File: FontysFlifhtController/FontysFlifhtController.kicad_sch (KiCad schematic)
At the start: 28 parts, among them J1 Conn_01x04, J10 Motor Control 3, J11 Motor Control 4, J12 Ultrasonic Sensor, J13 Battery Power, J2 Conn_01x04, J3 Conn_01x04, J4 Conn_01x04, J5 Conn_01x04, J6 Camera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

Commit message: Flight controller v2.0
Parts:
- removed C1: 4700uF, Capacitor_THT:CP_Radial_D13.0mm_P5.00mm, symbol Device:C_Polarized
- removed D1: LED_RGBA, LED_THT:LED_D5.0mm-4_RGB_Wide_Pins, symbol Device:LED_RGBA
- removed J3, J4, J5: Conn_01x04, Connector_JST:JST_PH_S4B-PH-K_1x04_P2.00mm_Horizontal, symbol Connector_Generic:Conn_01x04
- removed Q1: IRLZ34N, Package_TO_SOT_THT:TO-220-3_Vertical, symbol Simulation_SPICE:NMOS
- removed R2: 82, Resistor_THT:R_Axial_DIN0207_L6.3mm_D2.5mm_P7.62mm_Horizontal, symbol Device:R
- removed R3, R4: 12, Resistor_THT:R_Axial_DIN0207_L6.3mm_D2.5mm_P7.62mm_Horizontal, symbol Device:R
- removed SW1: Switch, Connector_PinHeader_2.54mm:PinHeader_1x03_P2.54mm_Vertical, symbol FlightController:Switch_APEM2
- removed U1: 4R7_Buck_Converter, FlightController:4R7_Buck_Converter, symbol FlightController:4R7_Buck_Converter
- added D1, D3, D4, D5: SS24, Diode_SMD:D_SOD-123F, symbol Diode:PMEG1020EH
- added D2: WS2812B (LED), LED_SMD:LED_WS2812B_PLCC4_5.0x5.0mm_P3.2mm, symbol LED:WS2812B
- added J14: RaspberryPi, Connector_PinHeader_2.54mm:PinHeader_1x01_P2.54mm_Vertical, symbol Connector_Generic:Conn_01x01
- added J3: SPI 1, Connector_JST:JST_PH_S6B-PH-K_1x06_P2.00mm_Horizontal, symbol Connector_Generic:Conn_01x06
- added J4: SPI 2, Connector_JST:JST_PH_S6B-PH-K_1x06_P2.00mm_Horizontal, symbol Connector_Generic:Conn_01x06
- J1: value Conn_01x04 -> I2C 1
- J2: value Conn_01x04 -> I2C 2
- J6: footprint Connector_JST:JST_EH_S5B-EH_1x05_P2.50mm_Horizontal -> Connector_JST:JST_PH_S5B-PH-K_1x05_P2.00mm_Horizontal
- R1: value R -> 1M; footprint Resistor_THT:R_Axial_DIN0207_L6.3mm_D2.5mm_P7.62mm_Horizontal -> Resistor_SMD:R_0805_2012Metric
- U2: footprint RF_Module:nRF24L01_Breakout -> Connector_PinHeader_2.54mm:PinHeader_2x04_P2.54mm_Vertical
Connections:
- net A6: now also J12.1 (Pin_1); no longer J12.3 (Pin_3)
- net D10: now also U2.4 (~{CSN}); no longer J6.2 (Pin_2)
- net D11: now also U2.6 (MOSI), J3.4 (Pin_4), J4.4 (Pin_4)
- net D12: now also U2.7 (MISO), J3.3 (Pin_3), J4.3 (Pin_3)
- net D13: now also U2.5 (SCK), J3.2 (Pin_2), J4.2 (Pin_2)
- net D3: now also J6.3 (Pin_3); no longer U2.3 (CE)
- net D4: now also J6.4 (Pin_4); no longer U2.4 (~{CSN})
- net D5: now also D2.4 (DIN); no longer U2.5 (SCK)
- net D6: now also J3.1 (Pin_1); no longer U2.6 (MOSI)
- net D7: now also J4.1 (Pin_1); no longer U2.7 (MISO)
- net D9: now also U2.3 (CE); no longer J6.3 (Pin_3)
- net GND: now also J12.3 (Pin_3), D2.3 (VSS), J3.6 (Pin_6), J4.6 (Pin_6); no longer J12.1 (Pin_1)
- net VIN: now reaches J13.1 (Pin_1)
- net VIN: now also A1.30 (VIN)
- net 5V: now reaches R1.2
- net 5V: now also A1.27 (+5V), D1.2 (A), D2.1 (VDD), D3.2 (A), D4.2 (A), D5.2 (A), J14.1 (Pin_1)
- net 3.3V: now reaches A1.17 (3V3)
- net 3.3V: now also J1.2 (Pin_2), J12.2 (Pin_2), J2.2 (Pin_2), J6.5 (Pin_5), J7.4 (Pin_4), U2.2 (VCC), J3.5 (Pin_5), J4.5 (Pin_5)
- net A2: now reaches A1.21 (A2)
- net A2: now also J10.3 (Pin_3)
- net D2: now reaches A1.5 (D2)
- net D2: now also J6.2 (Pin_2)
- net A7: no longer names the net of A1.26 (A7)
- net A7: no longer J10.3 (Pin_3)
- net D8: no longer names the net of A1.11 (D8)
- net D8: no longer J6.4 (Pin_4)
- removed net VCC: A1.30 (VIN), J1.2 (Pin_2), J10.2 (Pin_2), J11.2 (Pin_2), J12.2 (Pin_2), J2.2 (Pin_2), J6.5 (Pin_5), J7.4 (Pin_4), J8.2 (Pin_2), J9.2 (Pin_2), U2.2 (VCC)
- new net: D3.1 (K), J9.2 (Pin_2)
- new net: D4.1 (K), J10.2 (Pin_2)
- new net: D5.1 (K), J11.2 (Pin_2)
- new net: D1.1 (K), J8.2 (Pin_2)
- no-connect marks 9 -> 7
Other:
- note added: "I2C BUS and SPI BUS"
- note removed: "I2C BUS DEVICES"
- moved on the sheet: J13

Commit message: Add turn on/off functionality for the motors
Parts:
- added J5: Motors On/Off, Connector_JST:JST_PH_S4B-PH-K_1x04_P2.00mm_Horizontal, symbol Connector_Generic:Conn_01x04
- D1, D3, D4, D5: LCSC Part # (none) -> C908678
- D2: LCSC Part # (none) -> C2761795
- H1, H2, H3, H4: footprint MountingHole:MountingHole_2.7mm_M2.5 -> MountingHole:MountingHole_3.2mm_M3
- J1, J2: LCSC Part # (none) -> C157926
- J10, J11, J8, J9: LCSC Part # (none) -> C2932698
- J12: LCSC Part # (none) -> C157929
- J13: LCSC Part # (none) -> C474906
- J14: LCSC Part # (none) -> C7501259
- J3, J4: LCSC Part # (none) -> C157920
- J6: LCSC Part # (none) -> C157923
- J7: LCSC Part # (none) -> C2935975
- R1: LCSC Part # (none) -> C17514
- U2: LCSC Part # (none) -> C92271
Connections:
- net D5: now also J5.1 (Pin_1), J5.2 (Pin_2), J5.3 (Pin_3), J5.4 (Pin_4); no longer D2.4 (DIN)
- net A7: now reaches A1.26 (A7)
- net A7: now also D2.4 (DIN)
- no-connect marks 7 -> 6

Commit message: Improve board
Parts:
- removed J5: Motors On/Off, Connector_JST:JST_PH_S4B-PH-K_1x04_P2.00mm_Horizontal, symbol Connector_Generic:Conn_01x04
- added J15: Motor 2 On/Off, Connector_PinHeader_2.54mm:PinHeader_1x03_P2.54mm_Vertical, symbol Connector_Generic:Conn_01x03
- added J16: Motor 3 On/Off, Connector_PinHeader_2.54mm:PinHeader_1x03_P2.54mm_Vertical, symbol Connector_Generic:Conn_01x03
- added J17: Motor 4 On/Off, Connector_PinHeader_2.54mm:PinHeader_1x03_P2.54mm_Vertical, symbol Connector_Generic:Conn_01x03
- added J5: Motor 1 On/Off, Connector_PinHeader_2.54mm:PinHeader_1x03_P2.54mm_Vertical, symbol Connector_Generic:Conn_01x03
- H1, H2, H3, H4: footprint MountingHole:MountingHole_3.2mm_M3 -> MountingHole:MountingHole_2.7mm_M2.5
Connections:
- net 3.3V: now also J15.2 (Pin_2), J16.2 (Pin_2), J17.2 (Pin_2), J5.2 (Pin_2)
- net D5: now also J15.1 (Pin_1), J16.1 (Pin_1), J17.1 (Pin_1), J5.1 (Pin_1)
- net GND: now also J15.3 (Pin_3), J16.3 (Pin_3), J17.3 (Pin_3), J5.3 (Pin_3)
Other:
- note added: "I2C BUS, SPI BUS and Motors On/Off BUS"
- note removed: "I2C BUS and SPI BUS"
- moved on the sheet: J1, J2, J3, J4

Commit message: final changes
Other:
- note added: "FLIGHT CONTROLLER MONITORING"
- note added: "I2C BUS, SPI BUS, and Motors On/Off BUS"
- note added: "MOTOR CONTROL"
- note added: "POWER INPUT/OUTPUT"
- note added: "SENSORS"
- note removed: "ANALOG INPUTS"
- note removed: "DIGITAL INPUTS"
- note removed: "I2C BUS, SPI BUS and Motors On/Off BUS"
- note removed: "POWER INPUT"
- moved on the sheet: D2, J12, J13, J14, R1

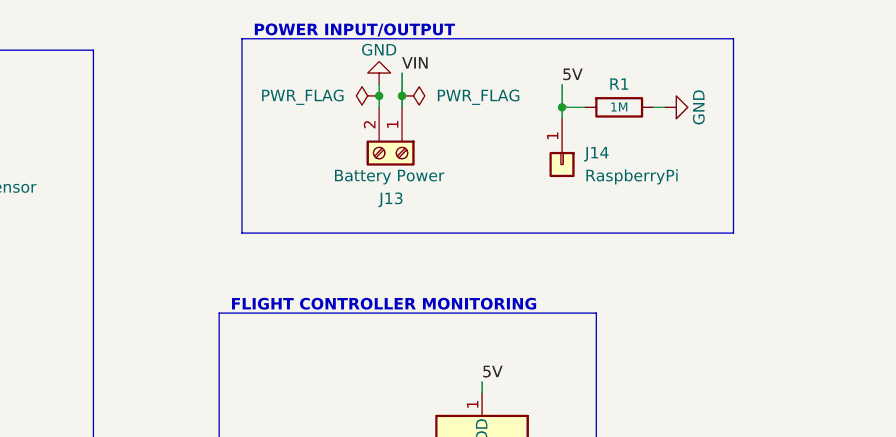
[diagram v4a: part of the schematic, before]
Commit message: add changes for feedback
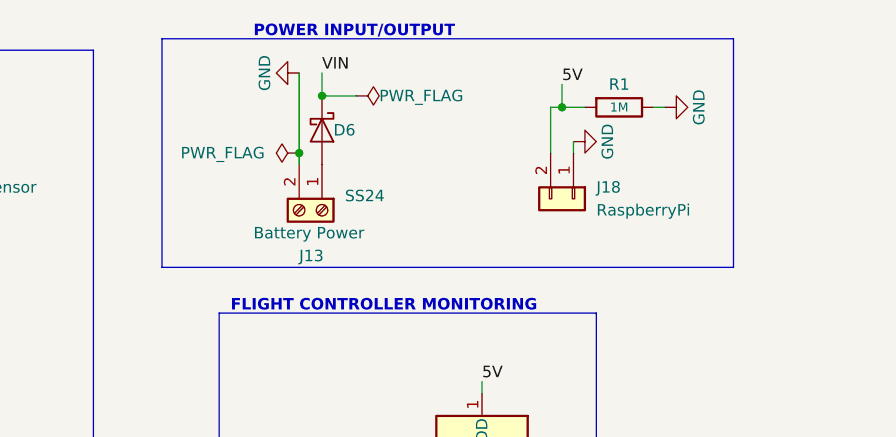
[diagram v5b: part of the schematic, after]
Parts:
- removed J14: RaspberryPi, Connector_PinHeader_2.54mm:PinHeader_1x01_P2.54mm_Vertical, symbol Connector_Generic:Conn_01x01
- added D6: SS24, Diode_SMD:D_SOD-123F, symbol Diode:PMEG1020EH
- added J18: RaspberryPi, Connector_PinHeader_2.54mm:PinHeader_1x02_P2.54mm_Vertical, symbol Connector_Generic:Conn_01x02
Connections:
- net 5V: now also J18.2 (Pin_2)
- net GND: now also J18.1 (Pin_1)
- net VIN: now also D6.1 (K); no longer J13.1 (Pin_1)
- new net: D6.2 (A), J13.1 (Pin_1)
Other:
- moved on the sheet: J13

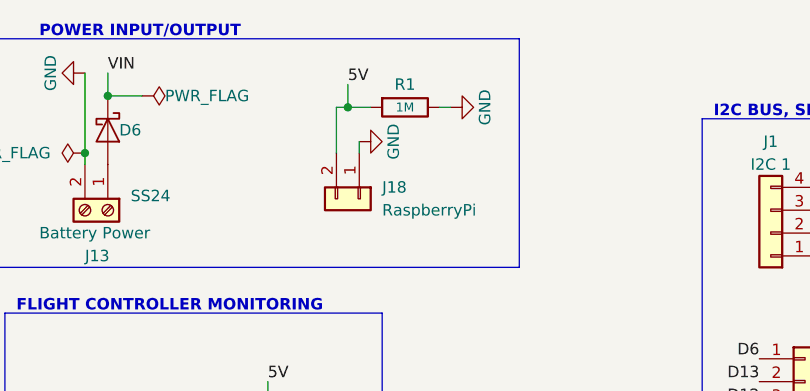
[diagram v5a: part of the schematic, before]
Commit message: change resistor label
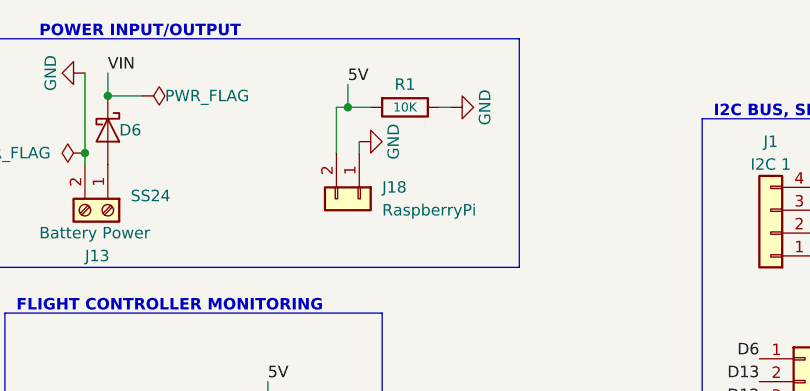
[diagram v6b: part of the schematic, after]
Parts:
- R1: value 1M -> 10K
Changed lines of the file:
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@@
       (effects (font (size 1.27 1.27)))
     )
-    (property "Value" "1M" (at 152.4 33.02 90)
+    (property "Value" "10K" (at 152.4 33.02 90)
       (effects (font (size 1 1)))
     )
